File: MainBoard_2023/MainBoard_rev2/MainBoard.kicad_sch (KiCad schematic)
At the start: 49 parts, among them J3 Conn_01x02, J4 Micro_SD_Card_Det_Hirose_DM3AT, J5 Micro_SD_Card_Det_Hirose_DM3AT, U1 ICP-10111, U3 BNO055, U4 XIAO, U5 Pi Pico 0, U6 Pi Pico 1

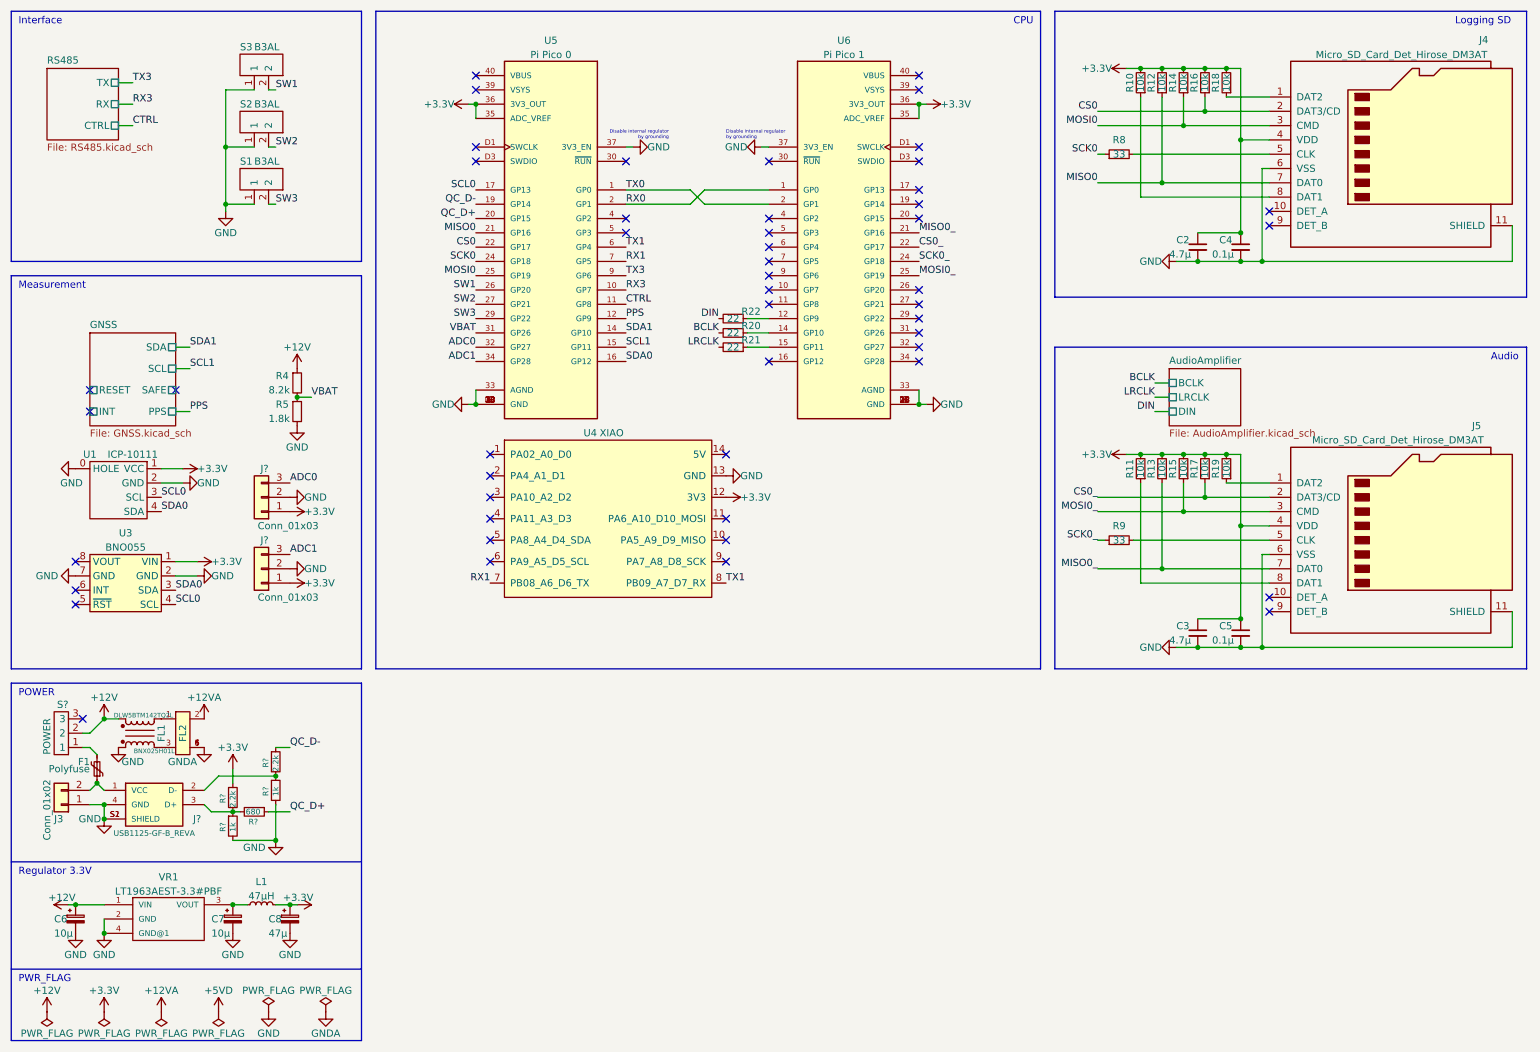
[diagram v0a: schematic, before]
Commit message: PCBファイルを作成
3Dモデルを割り当て　ブロックタイプエミフィルのパッドを小さくした
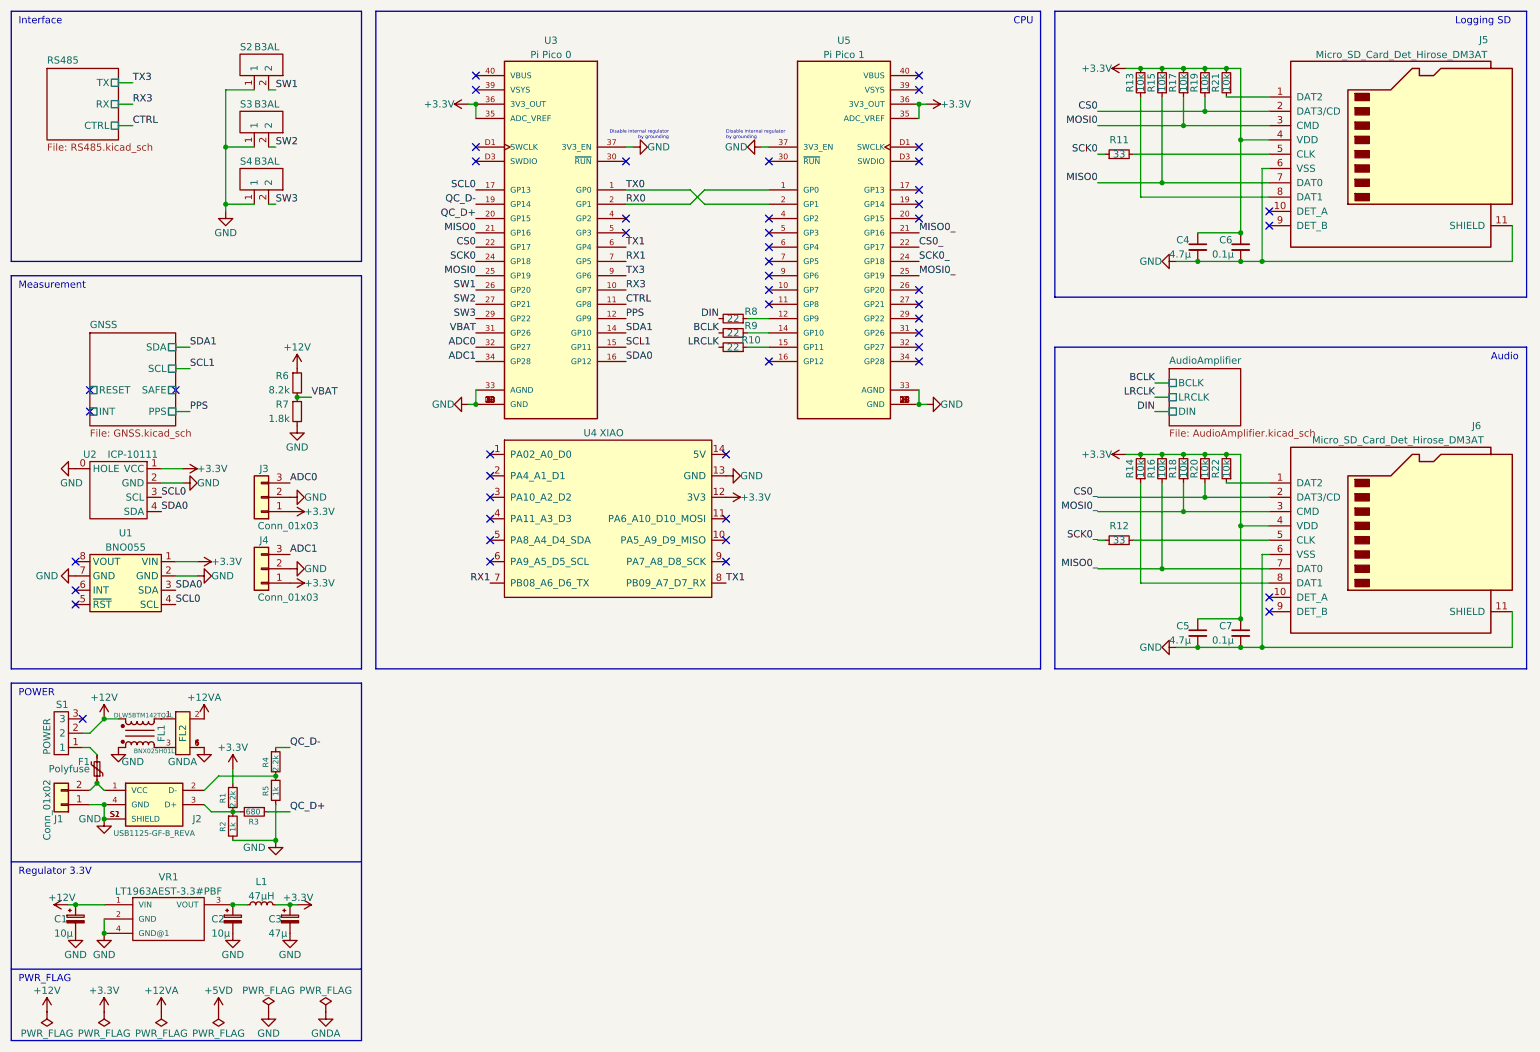
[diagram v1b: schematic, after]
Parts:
- J2: renamed from J?; footprint GCT_USB1125-GF-B_REVA -> USB1125-GF-B:USB1125-GF-B
- R1, R2, R3, R4, R5: renamed from R?; footprint (none) -> Resistor_SMD:R_0603_1608Metric_Pad0.98x0.95mm_HandSolder
- gave numbers to parts that had none: 3
- renumbered C6 to C1, C7 to C2, C8 to C3, C2 to C4, C3 to C5, C4 to C6, C5 to C7, J3 to J1, J4 to J5, J5 to J6, R21 to R10, R8 to R11, R9 to R12, R10 to R13, R11 to R14, R12 to R15, R13 to R16, R14 to R17, R15 to R18, R16 to R19, R17 to R20, R18 to R21, R19 to R22, R4 to R6, R5 to R7, R22 to R8, R20 to R9, S3 to S2, S2 to S3, S1 to S4, U3 to U1, U1 to U2, U5 to U3, U6 to U5

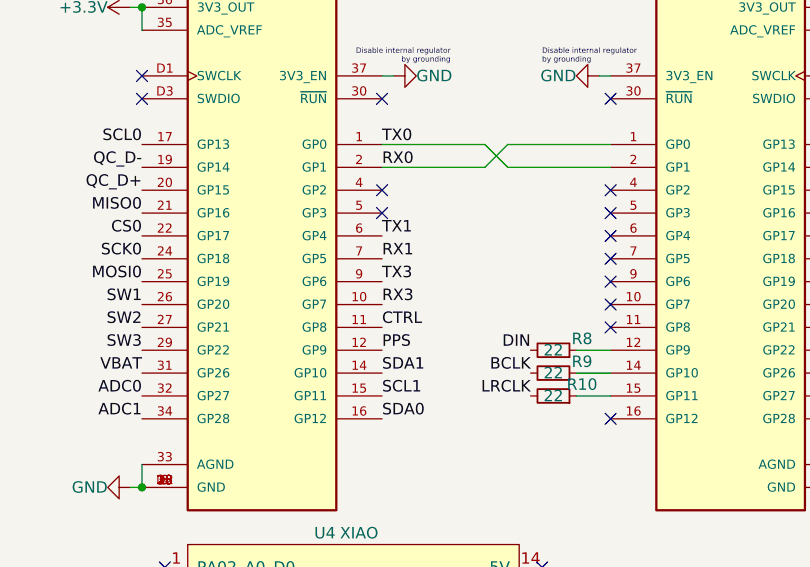
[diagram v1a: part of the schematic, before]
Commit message: メイン基板配置中
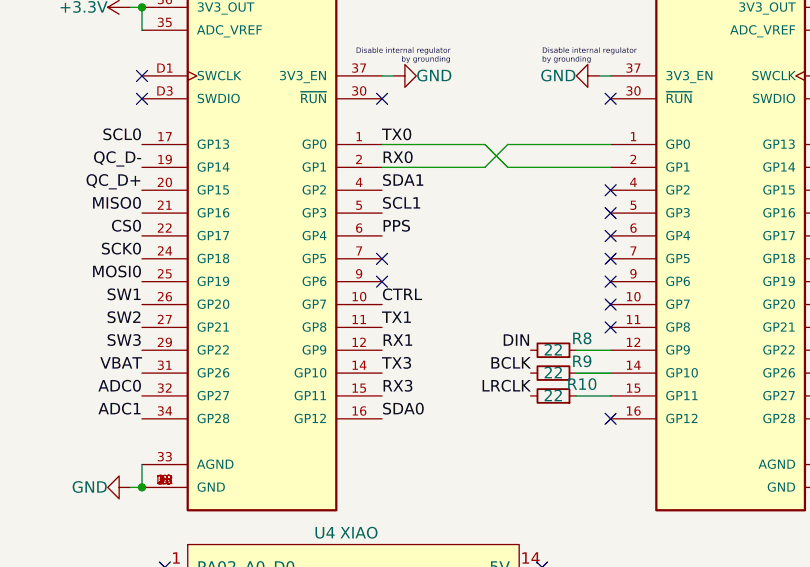
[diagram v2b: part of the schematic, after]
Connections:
- net CTRL: now also U3.10 (GP7); no longer U3.11 (GP8)
- net PPS: now also U3.6 (GP4); no longer U3.12 (GP9)
- net RX1: now also U3.12 (GP9); no longer U3.7 (GP5)
- net RX3: now also U3.15 (GP11); no longer U3.10 (GP7)
- net SCL1: now also U3.5 (GP3); no longer U3.15 (GP11)
- net SDA1: now also U3.4 (GP2); no longer U3.14 (GP10)
- net TX1: now also U3.11 (GP8); no longer U3.6 (GP4)
- net TX3: now also U3.14 (GP10); no longer U3.9 (GP6)
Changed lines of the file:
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@@
   (no_connect (at 237.49 49.53))
   (no_connect (at 175.26 48.26))
+  (no_connect (at 123.19 58.42))
   (no_connect (at 25.4 111.76))
   (no_connect (at 25.4 119.38))
@@
   (no_connect (at 96.52 27.94))
   (no_connect (at 96.52 25.4))
-  (no_connect (at 123.19 53.34))
   (no_connect (at 140.97 92.71))
   (no_connect (at 175.26 45.72))
@@
   (no_connect (at 123.19 40.64))
   (no_connect (at 175.26 27.94))
+  (no_connect (at 123.19 60.96))
   (no_connect (at 175.26 38.1))
   (no_connect (at 175.26 40.64))
-  (no_connect (at 123.19 50.8))
   (no_connect (at 148.59 66.04))
   (no_connect (at 175.26 68.58))
@@
     (effects (font (size 1.27 1.27)) (justify left bottom))
   )
-  (label "SDA1" (at 123.19 71.12 0)
+  (label "SDA1" (at 123.19 50.8 0)
     (effects (font (size 1.27 1.27)) (justify left bottom))
   )
@@
     (effects (font (size 1.27 1.27)) (justify left bottom))
   )
-  (label "PPS" (at 123.19 68.58 0)
+  (label "PPS" (at 123.19 55.88 0)
     (effects (font (size 1.27 1.27)) (justify left bottom))
   )
@@
     (effects (font (size 1.27 1.27)) (justify left bottom))
   )
-  (label "CTRL" (at 123.19 66.04 0)
+  (label "CTRL" (at 123.19 63.5 0)
     (effects (font (size 1.27 1.27)) (justify left bottom))
   )
@@
     (effects (font (size 1.27 1.27)) (justify left bottom))
   )
-  (label "RX1" (at 123.19 58.42 0)
+  (label "RX1" (at 123.19 68.58 0)
     (effects (font (size 1.27 1.27)) (justify left bottom))
   )
@@
     (effects (font (size 1.27 1.27)) (justify left bottom))
   )
-  (label "SCL1" (at 123.19 73.66 0)
+  (label "SCL1" (at 123.19 53.34 0)
     (effects (font (size 1.27 1.27)) (justify left bottom))
   )
@@
     (effects (font (size 1.27 1.27)) (justify left bottom))
   )
-  (label "RX3" (at 123.19 63.5 0)
+  (label "RX3" (at 123.19 73.66 0)
     (effects (font (size 1.27 1.27)) (justify left bottom))
   )
@@
     (effects (font (size 1.27 1.27)) (justify right bottom))
   )
-  (label "TX1" (at 123.19 55.88 0)
+  (label "TX1" (at 123.19 66.04 0)
     (effects (font (size 1.27 1.27)) (justify left bottom))
   )
@@
     (effects (font (size 1.27 1.27)) (justify right bottom))
   )
-  (label "TX3" (at 123.19 60.96 0)
+  (label "TX3" (at 123.19 71.12 0)
     (effects (font (size 1.27 1.27)) (justify left bottom))
   )
@@
       (reference "#PWR065") (unit 1) (value "GND") (footprint "")
     )
-    (path "/8f1460a1-bf5a-4b04-9570-47768632e84c/52657c9a-345d-4b1f-9a9f-ce48a8c2af51"
-      (reference "#PWR066") (unit 1) (value "GND") (footprint "")
-    )
     (path "/8f1460a1-bf5a-4b04-9570-47768632e84c/db9a786e-fa5d-43da-9f68-7a5cee5020c5"
-      (reference "#PWR067") (unit 1) (value "+3.3V") (footprint "")
+      (reference "#PWR066") (unit 1) (value "+3.3V") (footprint "")
     )
     (path "/8f1460a1-bf5a-4b04-9570-47768632e84c/fdc3842d-5a61-49c0-92bb-5068f6cb4949"
-      (reference "#PWR068") (unit 1) (value "GND") (footprint "")
+      (reference "#PWR067") (unit 1) (value "GND") (footprint "")
     )
     (path "/8f1460a1-bf5a-4b04-9570-47768632e84c/dbea8bbb-ddc1-4c51-9c19-cfd7994ee31a"
-      (reference "#PWR069") (unit 1) (value "+3.3V") (footprint "")
+      (reference "#PWR068") (unit 1) (value "+3.3V") (footprint "")
     )
     (path "/8f1460a1-bf5a-4b04-9570-47768632e84c/c87b84f5-c089-4c56-be25-82bd41d85f7f"
-      (reference "#PWR070") (unit 1) (value "+3.3V") (footprint "")
-    )
-    (path "/8f1460a1-bf5a-4b04-9570-47768632e84c/1c565027-a1f1-4bb4-a6e2-f6525dc27981"
-      (reference "#PWR071") (unit 1) (value "GND") (footprint "")
+      (reference "#PWR069") (unit 1) (value "+3.3V") (footprint "")
     )
     (path "/8f1460a1-bf5a-4b04-9570-47768632e84c/7fc821e7-f42d-46a4-9254-069a4e0af65b"
-      (reference "#PWR072") (unit 1) (value "+3.3V") (footprint "")
+      (reference "#PWR070") (unit 1) (value "+3.3V") (footprint "")
     )
     (path "/8f1460a1-bf5a-4b04-9570-47768632e84c/01ee3f92-b94d-4c04-a14e-6fb05a7f478e"
-      (reference "#PWR073") (unit 1) (value "GND") (footprint "")
+      (reference "#PWR071") (unit 1) (value "GND") (footprint "")
     )
     (path "/8f1460a1-bf5a-4b04-9570-47768632e84c/62a681d5-644d-4d1a-9ad1-c8249758fddc"
-      (reference "#PWR074") (unit 1) (value "GND") (footprint "")
+      (reference "#PWR072") (unit 1) (value "GND") (footprint "")
     )
     (path "/8f1460a1-bf5a-4b04-9570-47768632e84c/eab68a92-f1a9-4eee-9de8-f4535e88636e"
-      (reference "#PWR075") (unit 1) (value "+3.3V") (footprint "")
+      (reference "#PWR073") (unit 1) (value "+3.3V") (footprint "")
     )
     (path "/f85cf890-aa32-4504-b508-c8edf9387b44/fbd7d8ed-1c6b-458f-9861-f93d49171441"
-      (reference "#PWR076") (unit 1) (value "+3.3V") (footprint "")
+      (reference "#PWR074") (unit 1) (value "+3.3V") (footprint "")
     )
     (path "/f85cf890-aa32-4504-b508-c8edf9387b44/b20388f8-a389-4436-94c5-843cb9d8014c"
-      (reference "#PWR077") (unit 1) (value "GND") (footprint "")
+      (reference "#PWR075") (unit 1) (value "GND") (footprint "")
     )
     (path "/f85cf890-aa32-4504-b508-c8edf9387b44/ee679c5f-d77c-4caf-b1bf-b949dd040e42"
-      (reference "#PWR078") (unit 1) (value "GND") (footprint "")
+      (reference "#PWR076") (unit 1) (value "GND") (footprint "")
     )
     (path "/f85cf890-aa32-4504-b508-c8edf9387b44/500d9780-640e-4984-a151-de4cdbd81352"
-      (reference "#PWR079") (unit 1) (value "+3.3V") (footprint "")
+      (reference "#PWR077") (unit 1) (value "+3.3V") (footprint "")
     )
     (path "/f85cf890-aa32-4504-b508-c8edf9387b44/76569f07-b7b9-4af4-9355-8130ab3855ed"
-      (reference "#PWR080") (unit 1) (value "GND") (footprint "")
+      (reference "#PWR078") (unit 1) (value "GND") (footprint "")
     )
     (path "/f85cf890-aa32-4504-b508-c8edf9387b44/884c72e5-2a1b-4214-a69b-f68765424b9f"
-      (reference "#PWR081") (unit 1) (value "+3.3V") (footprint "")
+      (reference "#PWR079") (unit 1) (value "+3.3V") (footprint "")
     )
     (path "/f85cf890-aa32-4504-b508-c8edf9387b44/b56e815c-a00b-47d1-89e5-a538879cd94f"
-      (reference "#PWR082") (unit 1) (value "GND") (footprint "")
+      (reference "#PWR080") (unit 1) (value "GND") (footprint "")
     )
     (path "/f85cf890-aa32-4504-b508-c8edf9387b44/910d4006-9cb3-4209-a682-ea0226772706"
-      (reference "#PWR083") (unit 1) (value "GND") (footprint "")
+      (reference "#PWR081") (unit 1) (value "GND") (footprint "")
     )
     (path "/f85cf890-aa32-4504-b508-c8edf9387b44/33cc64bb-8da2-4a6f-845e-80162d41ecfa"
-      (reference "#PWR084") (unit 1) (value "+3.3V") (footprint "")
+      (reference "#PWR082") (unit 1) (value "+3.3V") (footprint "")
     )
     (path "/f85cf890-aa32-4504-b508-c8edf9387b44/c65e2d05-742a-49dc-bab5-27309d0aeb2f"
@@
       (reference "J9") (unit 1) (value "Conn_01x02") (footprint "Connector_PinHeader_2.54mm:PinHeader_1x02_P2.54mm_Vertical")
     )
+    (path "/8f1460a1-bf5a-4b04-9570-47768632e84c/d354dfe1-8189-4ec0-9dbc-e3c53881e1a5"
+      (reference "J10") (unit 1) (value "43814-6621") (footprint "Molex_6P6C_Right_Angle_TH_RJ11_Modular_Jack_Connector:Molex_6P6C_Right_Angle_TH_RJ11_Modular_Jack_Connector")
+    )
     (path "/c8d24f94-8173-4b16-af5a-1698d1012cbd"
       (reference "L1") (unit 1) (value "47μH") (footprint "NR10050T470M:NR10050T470M")
@@
       (reference "U7") (unit 1) (value "LTC1480CN8#PBF") (footprint "Package_DIP:DIP-8_W7.62mm_LongPads")
     )
-    (path "/8f1460a1-bf5a-4b04-9570-47768632e84c/c0fd1d72-29b0-4314-8336-0f9c5eed661f"
-      (reference "U8") (unit 1) (value "TM5RJ36450") (footprint "TM5RJ36450:TM5RJ36450")
-    )
-    (path "/8f1460a1-bf5a-4b04-9570-47768632e84c/4be4b442-1e3f-4d98-bd65-548012b17f32"
-      (reference "U9") (unit 1) (value "TM5RJ36450") (footprint "TM5RJ36450:TM5RJ36450")
-    )
     (path "/5d211f61-54bd-4b78-a50b-2f1f8ec59693"

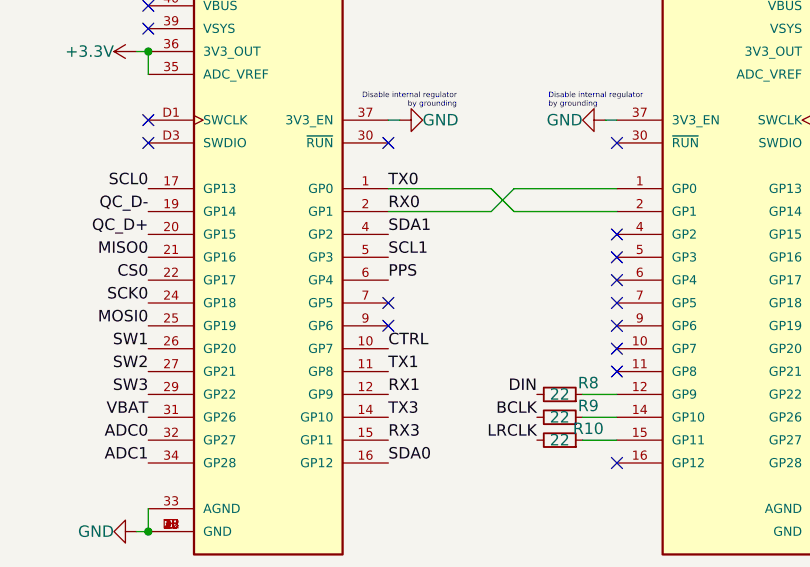
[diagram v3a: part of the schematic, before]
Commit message: yda142のFPを修正し配線
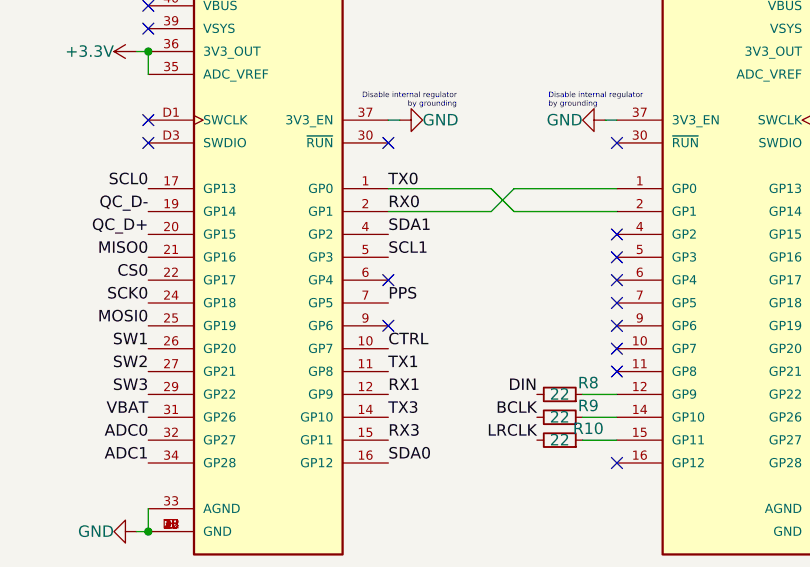
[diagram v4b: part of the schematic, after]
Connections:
- net PPS: now also U3.7 (GP5); no longer U3.6 (GP4)
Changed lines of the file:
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@@
   (no_connect (at 237.49 49.53))
   (no_connect (at 175.26 48.26))
-  (no_connect (at 123.19 58.42))
+  (no_connect (at 123.19 60.96))
   (no_connect (at 25.4 111.76))
   (no_connect (at 25.4 119.38))
@@
   (no_connect (at 123.19 40.64))
   (no_connect (at 175.26 27.94))
-  (no_connect (at 123.19 60.96))
+  (no_connect (at 123.19 55.88))
   (no_connect (at 175.26 38.1))
   (no_connect (at 175.26 40.64))
@@
     (effects (font (size 1.27 1.27)) (justify left bottom))
   )
-  (label "PPS" (at 123.19 55.88 0)
-    (effects (font (size 1.27 1.27)) (justify left bottom))
-  )
+  (label "PPS" (at 123.19 58.42 0)
+    (effects (font (size 1.27 1.27)) (justify left bottom))
+  )
